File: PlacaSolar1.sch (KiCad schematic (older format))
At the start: 10 parts, among them J1 Jack-DC, J2 Conn_01x02_Female, J3 Conn_01x02_Female, J4 Conn_01x15_Female, J5 Conn_01x15_Female, U1 L78L05_SO8

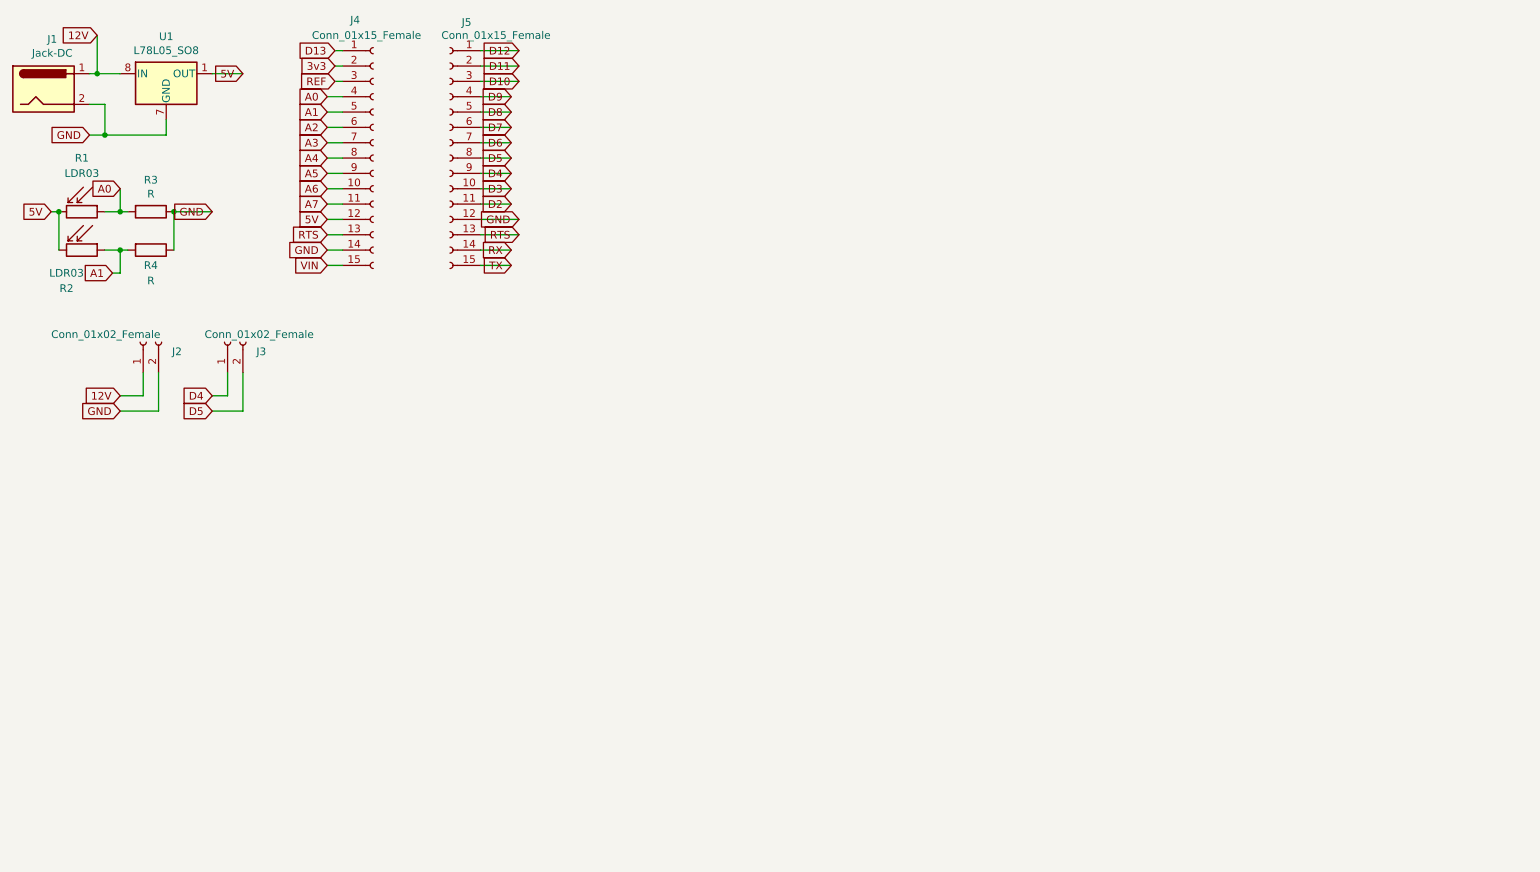
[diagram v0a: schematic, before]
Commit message: Atualizando esquemático
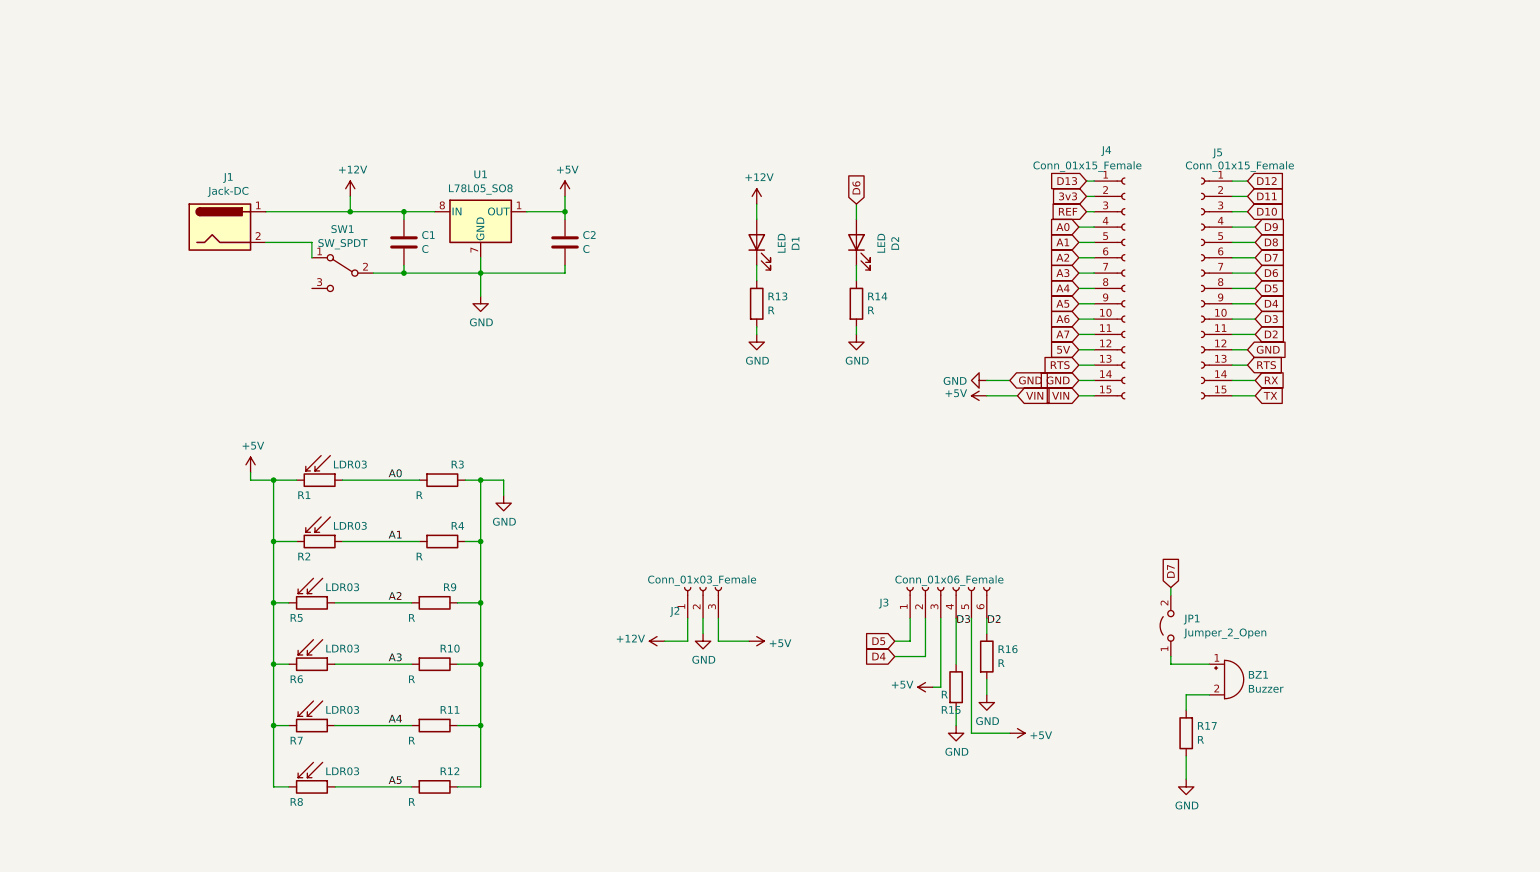
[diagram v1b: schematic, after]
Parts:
- removed J2, J3: Conn_01x02_Female, symbol Connector:Conn_01x02_Female
- added BZ1: Buzzer, symbol Device:Buzzer
- added C1, C2: C, symbol Device:C
- added D1, D2: LED, symbol Device:LED
- added J2: Conn_01x03_Female, symbol Connector:Conn_01x03_Female
- added J3: Conn_01x06_Female, symbol Connector:Conn_01x06_Female
- added JP1: Jumper_2_Open, Connector_PinHeader_2.54mm:PinHeader_1x02_P2.54mm_Vertical, symbol Jumper:Jumper_2_Open
- added R10, R11, R12, R13, R14, R15, R16, R17, R9: R, symbol Device:R
- added R5, R6, R7, R8: LDR03, OptoDevice:R_LDR_10x8.5mm_P7.6mm_Vertical, symbol Sensor_Optical:LDR03
- added SW1: SW_SPDT, symbol Switch:SW_SPDT
- R1: footprint OptoDevice:R_LDR_10x8.5mm_P7.6mm_Vertical -> TerminalBlock:TerminalBlock_bornier-2_P5.08mm
- R2: footprint OptoDevice:R_LDR_10x8.5mm_P7.6mm_Vertical -> TerminalBlock:TerminalBlock_bornier-3_P5.08mm
- U1: footprint Package_SO:SOIC-8_3.9x4.9mm_P1.27mm -> Package_TO_SOT_THT:TO-220-3_Vertical
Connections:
- net 5V: no longer R1.2, R2.2, U1.1 (OUT)
- net A2: now also R5.1, R9.2
- net A3: now also R10.2, R6.1
- net A4: now also R11.2, R7.1
- net A5: now also R12.2, R8.1
- net D2: now also J3.6 (Pin_6), R16.1
- net D3: now also J3.4 (Pin_4), R15.1
- net D4: now also J3.2 (Pin_2)
- net D5: now also J3.1 (Pin_1)
- net D6: now also D2.2 (A)
- net D7: now also JP1.2 (B)
- net GND: now also C1.2, C2.2, J2.2 (Pin_2), R10.1, R11.1, R12.1, R13.2, R14.2, R15.2, R16.2, R17.1, R9.1, SW1.2 (B); no longer J1.2
- net 12V renamed +12V
- net +12V: now also C1.1, D1.2 (A), J2.1 (Pin_1)
- net VIN renamed +5V
- net +5V: now also R1.2, R2.2, U1.1 (OUT), C2.1, J2.3 (Pin_3), J3.3 (Pin_3), J3.5 (Pin_5), R5.2, R6.2, R7.2, R8.2
- new net: J1.2, SW1.1 (A)
- new net: D1.1 (K), R13.1
- new net: D2.1 (K), R14.1
- new net: BZ1.1 (-), JP1.1 (A)
- new net: BZ1.2 (+), R17.2
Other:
- moved on the sheet: J1, J4, J5, R1, R2, R3, R4, U1

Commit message: Adicionando a footprint dos componentes
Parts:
- BZ1: footprint (none) -> Buzzer_Beeper:Buzzer_12x9.5RM7.6
- C1, C2: footprint (none) -> Capacitor_THT:CP_Radial_D5.0mm_P2.50mm
- D1, D2: footprint (none) -> LED_THT:LED_D5.0mm
- J1: footprint (none) -> Connector_BarrelJack:BarrelJack_Horizontal
- J2: footprint (none) -> TerminalBlock:TerminalBlock_bornier-3_P5.08mm
- J3: footprint (none) -> TerminalBlock:TerminalBlock_bornier-6_P5.08mm
- J4, J5: footprint (none) -> Connector_PinSocket_2.54mm:PinSocket_1x15_P2.54mm_Vertical
- R10, R11, R12, R13, R14, R15, R16, R17, R3, R4, R9: footprint (none) -> Resistor_THT:R_Axial_DIN0207_L6.3mm_D2.5mm_P10.16mm_Horizontal
- SW1: footprint (none) -> 2267077-2:TE_2267077-2
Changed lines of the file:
@@
 F 0 "J1" H 2107 2175 50  0000 C CNN
 F 1 "Jack-DC" H 2107 2084 50  0000 C CNN
-F 2 "" H 2100 1810 50  0001 C CNN
+F 2 "Connector_BarrelJack:BarrelJack_Horizontal" H 2100 1810 50  0001 C CNN
 F 3 "~" H 2100 1810 50  0001 C CNN
 	1    2050 1850
@@
 F 0 "C1" H 3365 1996 50  0000 L CNN
 F 1 "C" H 3365 1905 50  0000 L CNN
-F 2 "" H 3288 1800 50  0001 C CNN
+F 2 "Capacitor_THT:CP_Radial_D5.0mm_P2.50mm" H 3288 1800 50  0001 C CNN
 F 3 "~" H 3250 1950 50  0001 C CNN
 	1    3250 1950
@@
 F 0 "C2" H 4415 1996 50  0000 L CNN
 F 1 "C" H 4415 1905 50  0000 L CNN
-F 2 "" H 4338 1800 50  0001 C CNN
+F 2 "Capacitor_THT:CP_Radial_D5.0mm_P2.50mm" H 4338 1800 50  0001 C CNN
 F 3 "~" H 4300 1950 50  0001 C CNN
 	1    4300 1950
@@
 F 0 "SW1" H 2850 2435 50  0000 C CNN
 F 1 "SW_SPDT" H 2850 2344 50  0000 C CNN
-F 2 "" H 2850 2150 50  0001 C CNN
+F 2 "2267077-2:TE_2267077-2" H 2850 2150 50  0001 C CNN
 F 3 "~" H 2850 2150 50  0001 C CNN
 	1    2850 2150
@@
 F 0 "D1" H 5543 1695 50  0000 C CNN
 F 1 "LED" H 5543 1786 50  0000 C CNN
-F 2 "" H 5550 1950 50  0001 C CNN
+F 2 "LED_THT:LED_D5.0mm" H 5550 1950 50  0001 C CNN
 F 3 "~" H 5550 1950 50  0001 C CNN
 	1    5550 1950
@@
 F 0 "R13" H 5620 2396 50  0000 L CNN
 F 1 "R" H 5620 2305 50  0000 L CNN
-F 2 "" V 5480 2350 50  0001 C CNN
+F 2 "Resistor_THT:R_Axial_DIN0207_L6.3mm_D2.5mm_P10.16mm_Horizontal" V 5480 2350 50  0001 C CNN
 F 3 "~" H 5550 2350 50  0001 C CNN
 	1    5550 2350
@@
 F 0 "J5" H 8342 3135 50  0000 C CNN
 F 1 "Conn_01x15_Female" H 8200 3050 50  0000 C CNN
-F 2 "" H 8450 2250 50  0001 C CNN
+F 2 "Connector_PinSocket_2.54mm:PinSocket_1x15_P2.54mm_Vertical" H 8450 2250 50  0001 C CNN
 F 3 "~" H 8450 2250 50  0001 C CNN
 	1    8450 2250
@@
 F 0 "D2" H 6193 1695 50  0000 C CNN
 F 1 "LED" H 6193 1786 50  0000 C CNN
-F 2 "" H 6200 1950 50  0001 C CNN
+F 2 "LED_THT:LED_D5.0mm" H 6200 1950 50  0001 C CNN
 F 3 "~" H 6200 1950 50  0001 C CNN
 	1    6200 1950
@@
 F 0 "R14" H 6270 2396 50  0000 L CNN
 F 1 "R" H 6270 2305 50  0000 L CNN
-F 2 "" V 6130 2350 50  0001 C CNN
+F 2 "Resistor_THT:R_Axial_DIN0207_L6.3mm_D2.5mm_P10.16mm_Horizontal" V 6130 2350 50  0001 C CNN
 F 3 "~" H 6200 2350 50  0001 C CNN
 	1    6200 2350
@@
 F 0 "J4" H 7800 3150 50  0000 L CNN
 F 1 "Conn_01x15_Female" H 7350 3050 50  0000 L CNN
-F 2 "" H 7950 2250 50  0001 C CNN
+F 2 "Connector_PinSocket_2.54mm:PinSocket_1x15_P2.54mm_Vertical" H 7950 2250 50  0001 C CNN
 F 3 "~" H 7950 2250 50  0001 C CNN
 	1    7950 2250
@@
 F 0 "R16" H 7120 4696 50  0000 L CNN
 F 1 "R" H 7120 4605 50  0000 L CNN
-F 2 "" V 6980 4650 50  0001 C CNN
+F 2 "Resistor_THT:R_Axial_DIN0207_L6.3mm_D2.5mm_P10.16mm_Horizontal" V 6980 4650 50  0001 C CNN
 F 3 "~" H 7050 4650 50  0001 C CNN
 	1    7050 4650
@@
 F 0 "R15" H 6750 4700 50  0000 L CNN
 F 1 "R" H 6750 4800 50  0000 L CNN
-F 2 "" V 6780 4850 50  0001 C CNN
+F 2 "Resistor_THT:R_Axial_DIN0207_L6.3mm_D2.5mm_P10.16mm_Horizontal" V 6780 4850 50  0001 C CNN
 F 3 "~" H 6850 4850 50  0001 C CNN
 	1    6850 4850
@@
 F 0 "J3" V 6650 4600 50  0000 R CNN
 F 1 "Conn_01x06_Female" V 6800 4500 50  0000 R CNN
-F 2 "" H 6750 4200 50  0001 C CNN
+F 2 "TerminalBlock:TerminalBlock_bornier-6_P5.08mm" H 6750 4200 50  0001 C CNN
 F 3 "~" H 6750 4200 50  0001 C CNN
 	1    6750 4200
@@
 F 0 "R11" V 3350 5200 50  0000 C CNN
 F 1 "R" V 3550 4950 50  0000 C CNN
-F 2 "" V 3380 5100 50  0001 C CNN
+F 2 "Resistor_THT:R_Axial_DIN0207_L6.3mm_D2.5mm_P10.16mm_Horizontal" V 3380 5100 50  0001 C CNN
 F 3 "~" H 3450 5100 50  0001 C CNN
 	1    3450 5100
@@
 F 0 "R12" V 3350 5600 50  0000 C CNN
 F 1 "R" V 3550 5350 50  0000 C CNN
-F 2 "" V 3380 5500 50  0001 C CNN
+F 2 "Resistor_THT:R_Axial_DIN0207_L6.3mm_D2.5mm_P10.16mm_Horizontal" V 3380 5500 50  0001 C CNN
 F 3 "~" H 3450 5500 50  0001 C CNN
 	1    3450 5500
@@
 F 0 "R9" V 3350 4400 50  0000 C CNN
 F 1 "R" V 3550 4150 50  0000 C CNN
-F 2 "" V 3380 4300 50  0001 C CNN
+F 2 "Resistor_THT:R_Axial_DIN0207_L6.3mm_D2.5mm_P10.16mm_Horizontal" V 3380 4300 50  0001 C CNN
 F 3 "~" H 3450 4300 50  0001 C CNN
 	1    3450 4300
@@
 F 0 "R10" V 3350 4800 50  0000 C CNN
 F 1 "R" V 3550 4550 50  0000 C CNN
-F 2 "" V 3380 4700 50  0001 C CNN
+F 2 "Resistor_THT:R_Axial_DIN0207_L6.3mm_D2.5mm_P10.16mm_Horizontal" V 3380 4700 50  0001 C CNN
 F 3 "~" H 3450 4700 50  0001 C CNN
 	1    3450 4700
@@
 F 0 "BZ1" H 8752 4829 50  0000 L CNN
 F 1 "Buzzer" H 8752 4738 50  0000 L CNN
-F 2 "" V 8575 4900 50  0001 C CNN
+F 2 "Buzzer_Beeper:Buzzer_12x9.5RM7.6" V 8575 4900 50  0001 C CNN
 F 3 "~" V 8575 4900 50  0001 C CNN
 	1    8600 4800
@@
 F 0 "J2" V 5046 4348 50  0000 L CNN
 F 1 "Conn_01x03_Female" V 5250 3850 50  0000 L CNN
-F 2 "" H 5200 4200 50  0001 C CNN
+F 2 "TerminalBlock:TerminalBlock_bornier-3_P5.08mm" H 5200 4200 50  0001 C CNN
 F 3 "~" H 5200 4200 50  0001 C CNN
 	1    5200 4200
@@
 F 0 "R3" V 3400 3600 50  0000 C CNN
 F 1 "R" V 3600 3350 50  0000 C CNN
-F 2 "" V 3430 3500 50  0001 C CNN
+F 2 "Resistor_THT:R_Axial_DIN0207_L6.3mm_D2.5mm_P10.16mm_Horizontal" V 3430 3500 50  0001 C CNN
 F 3 "~" H 3500 3500 50  0001 C CNN
 	1    3500 3500
@@
 F 0 "R4" V 3400 4000 50  0000 C CNN
 F 1 "R" V 3600 3750 50  0000 C CNN
-F 2 "" V 3430 3900 50  0001 C CNN
+F 2 "Resistor_THT:R_Axial_DIN0207_L6.3mm_D2.5mm_P10.16mm_Horizontal" V 3430 3900 50  0001 C CNN
 F 3 "~" H 3500 3900 50  0001 C CNN
 	1    3500 3900
@@
 F 0 "R17" H 8280 5104 50  0000 R CNN
 F 1 "R" H 8280 5195 50  0000 R CNN
-F 2 "" V 8280 5150 50  0001 C CNN
+F 2 "Resistor_THT:R_Axial_DIN0207_L6.3mm_D2.5mm_P10.16mm_Horizontal" V 8280 5150 50  0001 C CNN
 F 3 "~" H 8350 5150 50  0001 C CNN
 	1    8350 5150

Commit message: Adicionando botão de reset ao esquemático
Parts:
- added R18: R, Resistor_THT:R_Axial_DIN0207_L6.3mm_D2.5mm_P10.16mm_Horizontal, symbol Device:R
- added SW2: SW_Push, Button_Switch_THT:SW_PUSH_6mm, symbol Switch:SW_Push
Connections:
- net +5V: now also R18.1
- net GND: now also SW2.2
- net RTS: now also R18.2, SW2.1
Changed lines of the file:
@@
 	-1   0    0    1
 $EndComp
+$Comp
+L Switch:SW_Push SW2
+U 1 1 613C8742
+P 10050 4000
+F 0 "SW2" V 10004 4148 50  0000 L CNN
+F 1 "SW_Push" V 10095 4148 50  0000 L CNN
+F 2 "Button_Switch_THT:SW_PUSH_6mm" H 10050 4200 50  0001 C CNN
+F 3 "~" H 10050 4200 50  0001 C CNN
+	1    10050 4000
+	0    1    1    0
+$EndComp
+$Comp
+L power:+5V #PWR019
+U 1 1 613CCD35
+P 10050 3150
+F 0 "#PWR019" H 10050 3000 50  0001 C CNN
+F 1 "+5V" H 10065 3323 50  0000 C CNN
+F 2 "" H 10050 3150 50  0001 C CNN
+F 3 "" H 10050 3150 50  0001 C CNN
+	1    10050 3150
+	1    0    0    -1
+$EndComp
+$Comp
+L power:GND #PWR020
+U 1 1 613CD321
+P 10050 4450
+F 0 "#PWR020" H 10050 4200 50  0001 C CNN
+F 1 "GND" H 10055 4277 50  0000 C CNN
+F 2 "" H 10050 4450 50  0001 C CNN
+F 3 "" H 10050 4450 50  0001 C CNN
+	1    10050 4450
+	1    0    0    -1
+$EndComp
+$Comp
+L Device:R R18
+U 1 1 613D230B
+P 10050 3400
+F 0 "R18" H 10120 3446 50  0000 L CNN
+F 1 "R" H 10120 3355 50  0000 L CNN
+F 2 "Resistor_THT:R_Axial_DIN0207_L6.3mm_D2.5mm_P10.16mm_Horizontal" V 9980 3400 50  0001 C CNN
+F 3 "~" H 10050 3400 50  0001 C CNN
+	1    10050 3400
+	1    0    0    -1
+$EndComp
+Wire Wire Line
+	10050 3800 10050 3700
+Text GLabel 9850 3700 0    50   Input ~ 0
+RTS
+Wire Wire Line
+	10050 3250 10050 3150
+Wire Wire Line
+	10050 4200 10050 4450
+Wire Wire Line
+	10050 3700 9850 3700
+Connection ~ 10050 3700
+Wire Wire Line
+	10050 3700 10050 3550
 $EndSCHEMATC

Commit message: Corrigindo footprint dos LDRs
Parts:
- R5, R6, R7, R8: footprint OptoDevice:R_LDR_10x8.5mm_P7.6mm_Vertical -> TerminalBlock:TerminalBlock_bornier-2_P5.08mm
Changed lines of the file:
@@
 F 0 "R7" V 2750 5000 50  0000 C CNN
 F 1 "LDR03" V 2550 5300 50  0000 C CNN
-F 2 "OptoDevice:R_LDR_10x8.5mm_P7.6mm_Vertical" V 2825 5100 50  0001 C CNN
+F 2 "TerminalBlock:TerminalBlock_bornier-2_P5.08mm" V 2825 5100 50  0001 C CNN
 F 3 "http://www.elektronica-componenten.nl/WebRoot/StoreNL/Shops/61422969/54F1/BA0C/C664/31B9/2173/C0A8/2AB9/2AEF/LDR03IMP.pdf" H 2650 5050 50  0001 C CNN
 	1    2650 5100
@@
 F 0 "R8" V 2750 5400 50  0000 C CNN
 F 1 "LDR03" V 2550 5700 50  0000 C CNN
-F 2 "OptoDevice:R_LDR_10x8.5mm_P7.6mm_Vertical" V 2825 5500 50  0001 C CNN
+F 2 "TerminalBlock:TerminalBlock_bornier-2_P5.08mm" V 2825 5500 50  0001 C CNN
 F 3 "http://www.elektronica-componenten.nl/WebRoot/StoreNL/Shops/61422969/54F1/BA0C/C664/31B9/2173/C0A8/2AB9/2AEF/LDR03IMP.pdf" H 2650 5450 50  0001 C CNN
 	1    2650 5500
@@
 F 0 "R5" V 2750 4200 50  0000 C CNN
 F 1 "LDR03" V 2550 4500 50  0000 C CNN
-F 2 "OptoDevice:R_LDR_10x8.5mm_P7.6mm_Vertical" V 2825 4300 50  0001 C CNN
+F 2 "TerminalBlock:TerminalBlock_bornier-2_P5.08mm" V 2825 4300 50  0001 C CNN
 F 3 "http://www.elektronica-componenten.nl/WebRoot/StoreNL/Shops/61422969/54F1/BA0C/C664/31B9/2173/C0A8/2AB9/2AEF/LDR03IMP.pdf" H 2650 4250 50  0001 C CNN
 	1    2650 4300
@@
 F 0 "R6" V 2750 4600 50  0000 C CNN
 F 1 "LDR03" V 2550 4900 50  0000 C CNN
-F 2 "OptoDevice:R_LDR_10x8.5mm_P7.6mm_Vertical" V 2825 4700 50  0001 C CNN
+F 2 "TerminalBlock:TerminalBlock_bornier-2_P5.08mm" V 2825 4700 50  0001 C CNN
 F 3 "http://www.elektronica-componenten.nl/WebRoot/StoreNL/Shops/61422969/54F1/BA0C/C664/31B9/2173/C0A8/2AB9/2AEF/LDR03IMP.pdf" H 2650 4650 50  0001 C CNN
 	1    2650 4700
